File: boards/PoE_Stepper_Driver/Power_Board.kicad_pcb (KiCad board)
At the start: 2 copper layers, 86.4 x 40.6 mm, 13 parts, among them J5 48V In, J6 12V, 3V3 Out, U4 NCP1117, U5 E48SC12010

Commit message: finished power board fr
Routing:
- net +12V: track 11.1 -> 26.5 mm
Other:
- outline, holes or cut-outs redrawn
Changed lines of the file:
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@@
   (general
     (thickness 1.6)
-    (drawings 6)
-    (tracks 20)
+    (drawings 10)
+    (tracks 23)
     (zones 0)
     (modules 13)
@@
   )
   (setup
-    (last_trace_width 0.508)
+    (last_trace_width 1.524)
     (user_trace_width 0.2032)
     (user_trace_width 0.254)
@@
     (user_trace_width 1.524)
     (trace_clearance 0.2)
-    (zone_clearance 0.254)
+    (zone_clearance 0.127)
     (zone_45_only no)
     (trace_min 0.2)
@@
     )
   )
+  (gr_arc (start 92.837 22.352) (end 94.107 22.352) (angle -90) (layer Edge.Cuts) (width 0.05))
+  (gr_arc (start 92.837 60.452) (end 92.837 61.722) (angle -90) (layer Edge.Cuts) (width 0.05))
+  (gr_arc (start 9.017 60.452) (end 7.747 60.452) (angle -90) (layer Edge.Cuts) (width 0.05))
+  (gr_arc (start 9.017 22.352) (end 9.017 21.082) (angle -90) (layer Edge.Cuts) (width 0.05))
   (dimension 40.64 (width 0.15) (layer Dwgs.User)
     (gr_text "1.6000 in" (at -3.713 41.402 90) (layer Dwgs.User)
@@
     (arrow2b (pts (xy 7.747 13.462) (xy 8.873504 12.875579)))
   )
-  (gr_line (start 7.747 61.722) (end 7.747 21.082) (layer Edge.Cuts) (width 0.05))
-  (gr_line (start 94.107 61.722) (end 7.747 61.722) (layer Edge.Cuts) (width 0.05))
-  (gr_line (start 94.107 21.082) (end 94.107 61.722) (layer Edge.Cuts) (width 0.05))
-  (gr_line (start 7.747 21.082) (end 94.107 21.082) (layer Edge.Cuts) (width 0.05))
+  (gr_line (start 7.747 60.452) (end 7.747 22.352) (layer Edge.Cuts) (width 0.05))
+  (gr_line (start 92.837 61.722) (end 9.017 61.722) (layer Edge.Cuts) (width 0.05))
+  (gr_line (start 94.107 22.352) (end 94.107 60.452) (layer Edge.Cuts) (width 0.05))
+  (gr_line (start 9.017 21.082) (end 92.837 21.082) (layer Edge.Cuts) (width 0.05))
   (segment (start 81.051 37.084) (end 87.351 37.084) (width 1.524) (layer F.Cu) (net 2))
   (segment (start 85.48 35.213) (end 87.351 37.084) (width 1.27) (layer F.Cu) (net 2))
@@
   (segment (start 74.817 39.384) (end 81.051 39.384) (width 1.524) (layer F.Cu) (net 5))
   (segment (start 74.041 38.608) (end 74.817 39.384) (width 1.524) (layer F.Cu) (net 5))
+  (segment (start 69.889 34.798) (end 74.041 34.798) (width 1.524) (layer F.Cu) (net 5))
+  (segment (start 63.627 28.536) (end 69.889 34.798) (width 1.524) (layer F.Cu) (net 5))
+  (segment (start 63.627 26.162) (end 63.627 28.536) (width 1.524) (layer F.Cu) (net 5))
   (via (at 81.026 29.464) (size 0.8) (drill 0.4) (layers F.Cu B.Cu) (net 7))
   (segment (start 81.035 29.455) (end 81.026 29.464) (width 0.254) (layer F.Cu) (net 7))
@@
   (segment (start 76.971 28.194) (end 78.985 28.194) (width 0.508) (layer F.Cu) (net 8))
   (zone (net 1) (net_name VOUT-) (layer B.Cu) (hatch edge 0.508)
+    (priority 1)
     (connect_pads yes (clearance 0.127))
     (min_thickness 0.254)
@@
     (polygon
       (pts
-        (xy 49.657 80.772) (xy -4.953 80.772) (xy -4.953 -10.668) (xy 49.657 -10.668)
+        (xy 49.657 62.992) (xy -4.953 62.992) (xy -4.953 18.542) (xy 49.657 18.542)
       )
     )
   )
   (zone (net 3) (net_name VOUT+) (layer F.Cu) (hatch edge 0.508)
+    (priority 1)
     (connect_pads yes (clearance 0.254))
     (min_thickness 0.254)
@@
     (polygon
       (pts
-        (xy 49.657 80.772) (xy -4.953 80.772) (xy -4.953 -10.668) (xy 49.657 -10.668)
+        (xy 49.657 62.992) (xy -4.953 62.992) (xy -4.953 18.542) (xy 49.657 18.542)
       )
     )
@@
     (polygon
       (pts
-        (xy 104.267 80.772) (xy 49.657 80.772) (xy 49.657 -10.668) (xy 104.267 -10.668)
+        (xy 104.267 62.992) (xy 49.657 62.992) (xy 49.657 18.542) (xy 104.267 18.542)
       )
     )
@@
     (polygon
       (pts
-        (xy 104.267 80.772) (xy 49.657 80.772) (xy 49.657 -10.668) (xy 104.267 -10.668)
+        (xy 104.267 62.992) (xy 49.657 62.992) (xy 49.657 18.542) (xy 104.267 18.542)
       )
     )

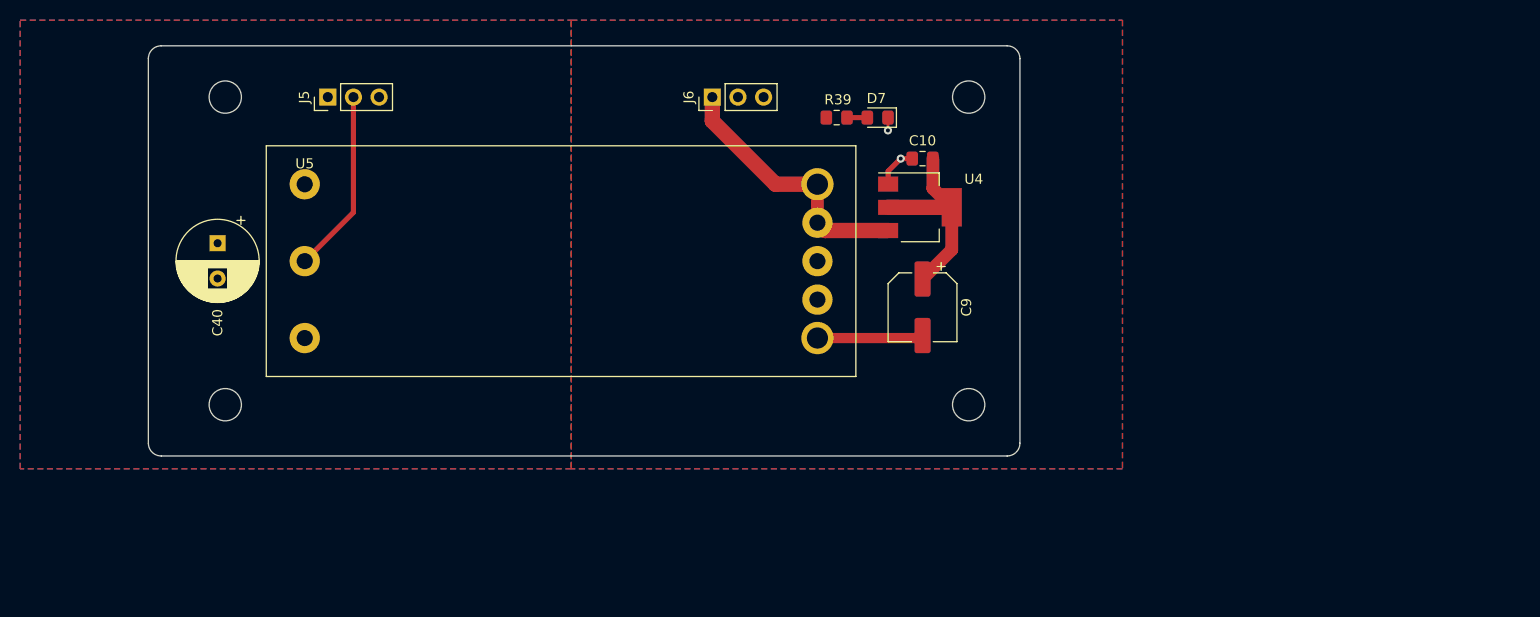
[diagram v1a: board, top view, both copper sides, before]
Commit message: done routing phy signals to mcu
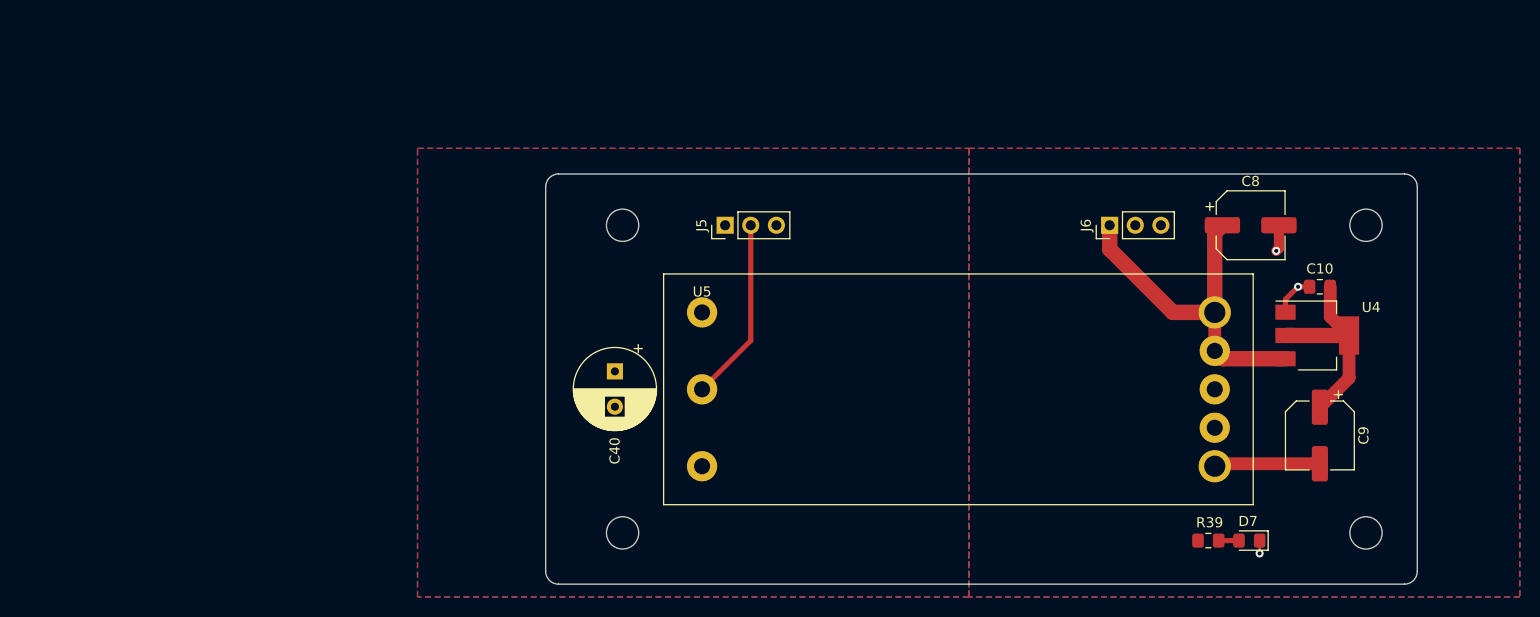
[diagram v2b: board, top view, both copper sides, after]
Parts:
- removed the REF** at (15.4, 26.2)
- removed the REF** at (15.4, 56.6)
- removed the REF** at (89.0, 56.6)
- added C8: 10uF, Capacitor_SMD:CP_Elec_6.3x5.4, F.Cu at (117.0, 38.9)
- added REF**: MountingHole_3.2mm_M3, MountingHole:MountingHole_3.2mm_M3, F.Cu at (54.7, 38.9)
- added REF**: MountingHole_3.2mm_M3, MountingHole:MountingHole_3.2mm_M3, F.Cu at (54.7, 69.3)
- added REF**: MountingHole_3.2mm_M3, MountingHole:MountingHole_3.2mm_M3, F.Cu at (128.4, 69.3)
- moved D7 55.8 mm to (116.8, 70.1)
- moved R39 55.8 mm to (112.8, 70.1)
- moved C10 41.4 mm to (123.8, 45.0)
- moved C40 41.4 mm to (54.0, 53.3)
- moved C9 41.4 mm to (123.8, 59.7)
- moved J5 41.4 mm to (64.9, 38.9)
- moved U4 41.4 mm to (123.6, 49.8)
- moved J6 41.4 mm to (103.0, 38.9)
- moved U5 41.4 mm to (62.6, 47.5)
- moved REF** 41.4 mm to (128.4, 38.9)
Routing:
- net +12V: track 26.5 -> 35.5 mm
- net GND: track 16.0 -> 18.6 mm, vias 2 -> 3

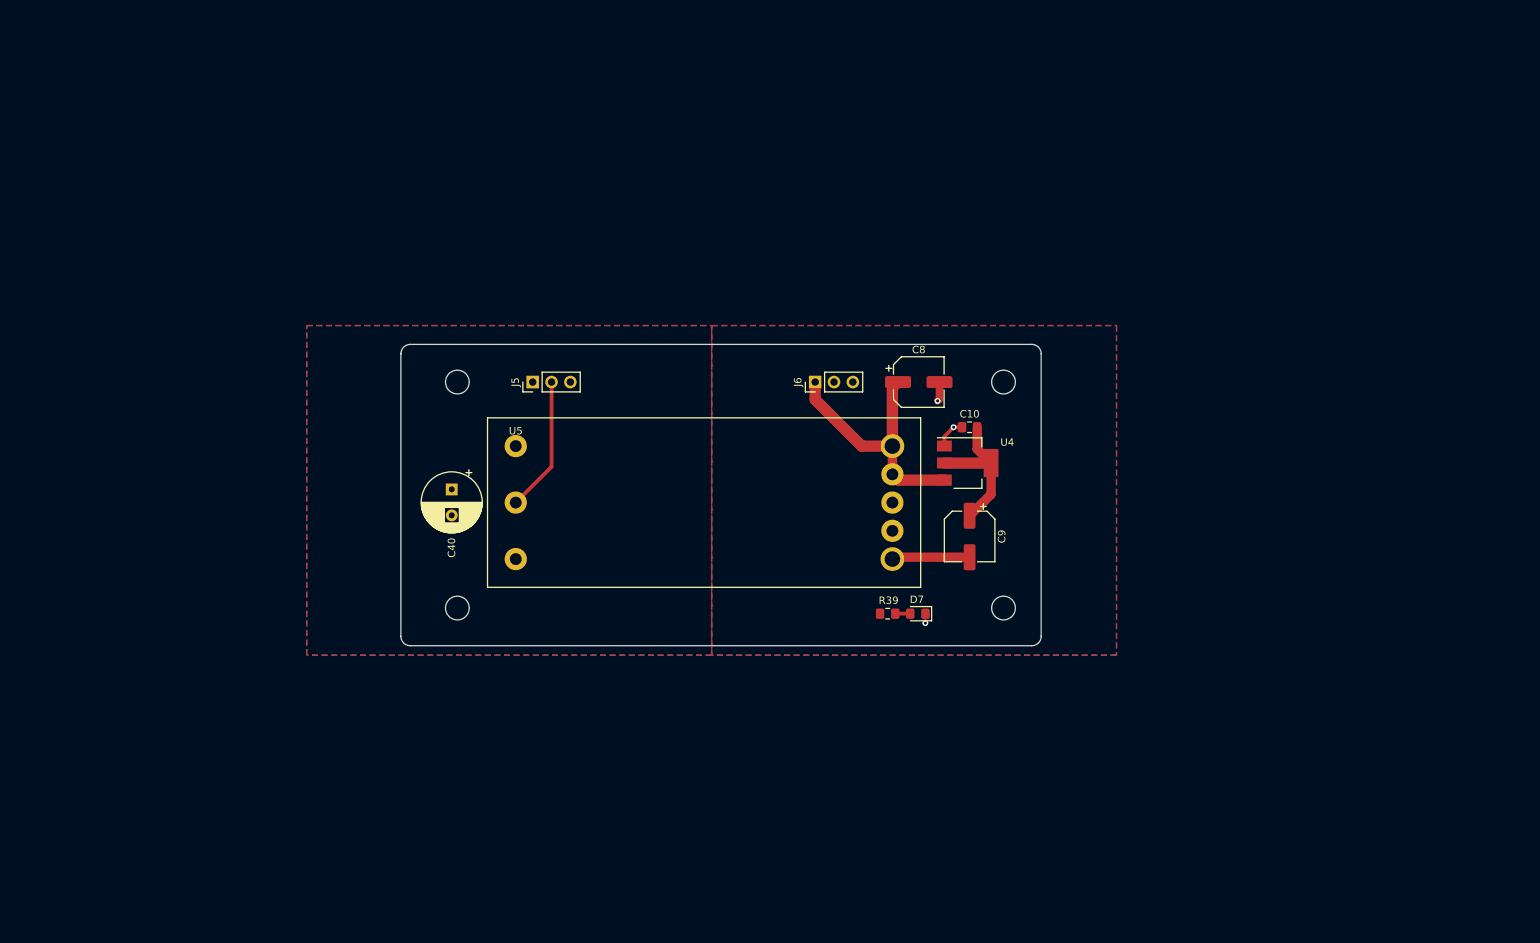
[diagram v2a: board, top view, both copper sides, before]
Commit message: added silkscreen info
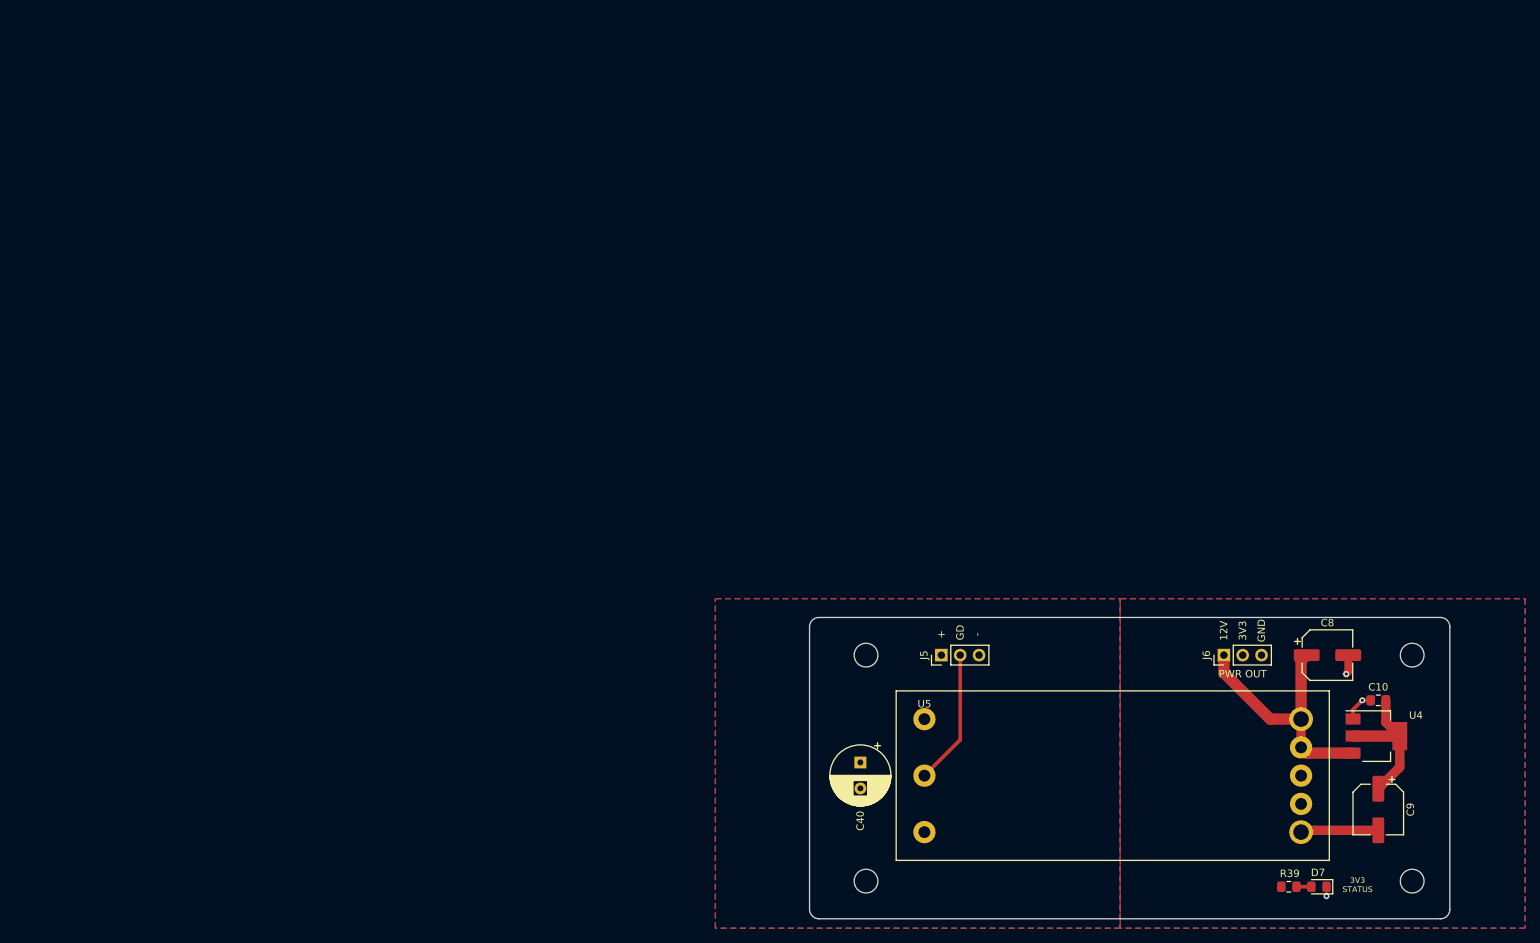
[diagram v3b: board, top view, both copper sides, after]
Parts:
- removed the REF** at (54.7, 38.9)
- removed the REF** at (54.7, 69.3)
- removed the REF** at (128.4, 69.3)
- added REF**: MountingHole_3.2mm_M3, MountingHole:MountingHole_3.2mm_M3, F.Cu at (109.9, 75.7)
- added REF**: MountingHole_3.2mm_M3, MountingHole:MountingHole_3.2mm_M3, F.Cu at (109.9, 106.2)
- added REF**: MountingHole_3.2mm_M3, MountingHole:MountingHole_3.2mm_M3, F.Cu at (183.5, 106.2)
- J5: value 48V In -> PWR IN
- J6: value 12V, 3V3 Out -> PWR OUT
- moved U5 66.3 mm to (117.7, 84.3)
- moved C10 66.3 mm to (178.9, 81.8)
- moved C40 66.3 mm to (109.1, 90.2)
- moved C8 66.3 mm to (172.1, 75.7)
- moved C9 66.3 mm to (178.9, 96.5)
- moved J6 66.3 mm to (158.1, 75.7)
- moved U4 66.3 mm to (178.7, 86.6)
- moved J5 66.3 mm to (120.0, 75.7)
- moved REF** 66.3 mm to (183.5, 75.7)
- moved D7 65.4 mm to (170.9, 106.9)
- moved R39 65.4 mm to (166.9, 106.9)
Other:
- board text added: "3V3 STATUS"

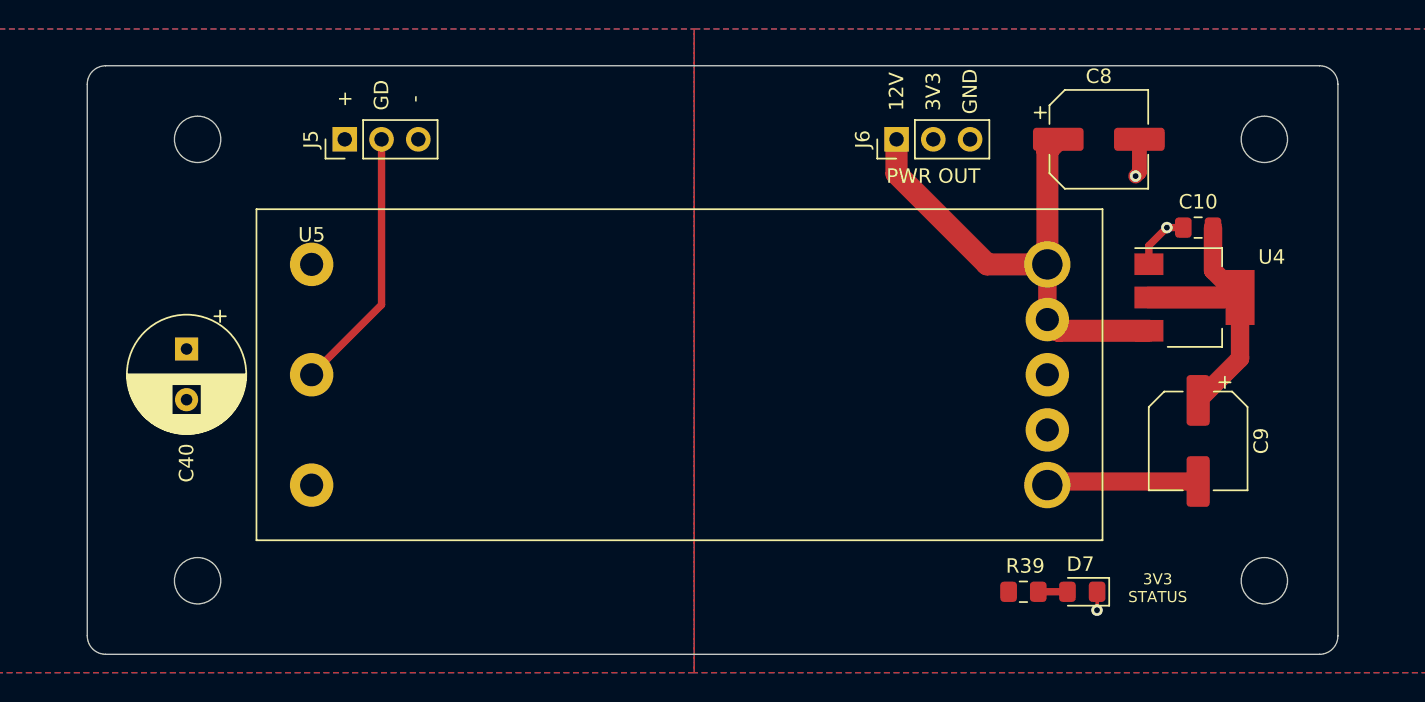
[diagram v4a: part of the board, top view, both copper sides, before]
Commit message: made rev2 board changes
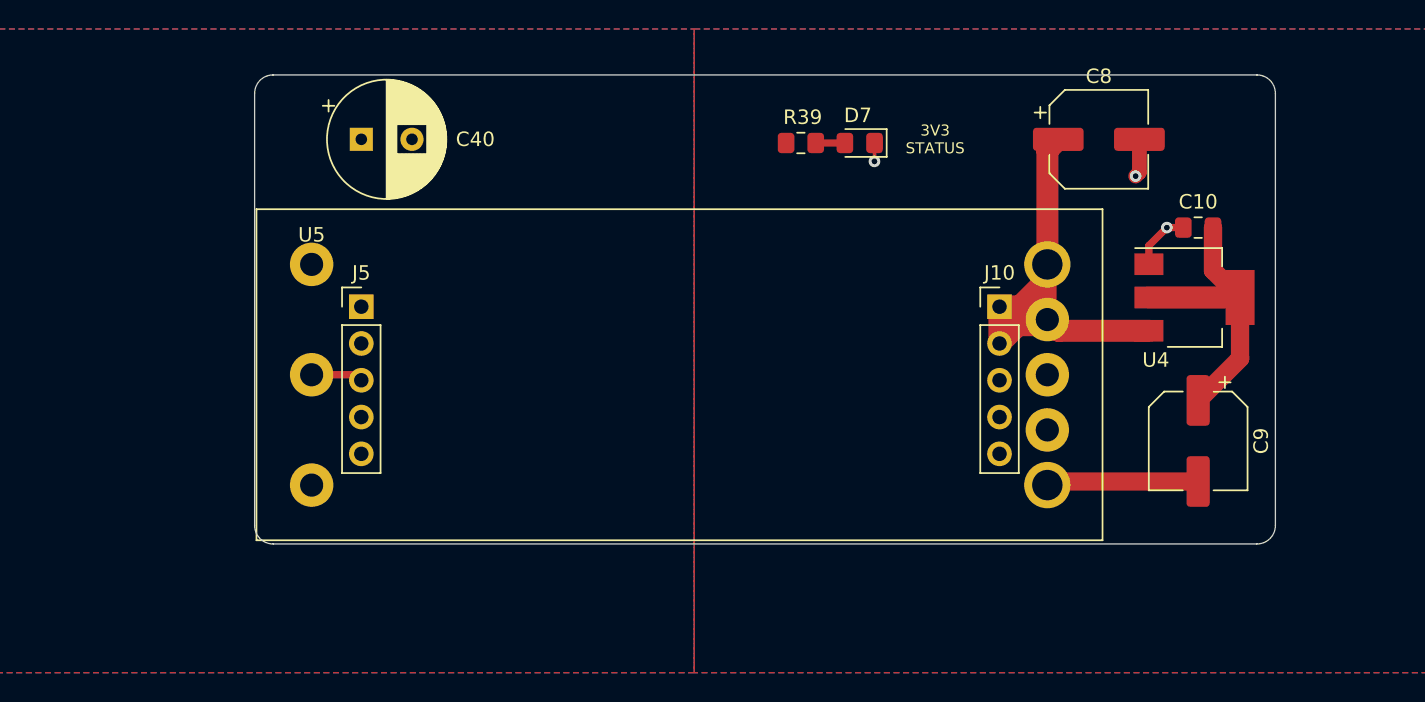
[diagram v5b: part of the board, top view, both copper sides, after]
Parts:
- removed J6: PWR OUT, Connector_PinHeader_2.54mm:PinHeader_1x03_P2.54mm_Vertical
- removed REF** (x4): MountingHole_3.2mm_M3, MountingHole:MountingHole_3.2mm_M3
- added J10: Converter Output, Connector_PinHeader_2.54mm:PinHeader_1x05_P2.54mm_Vertical, F.Cu at (165.2, 87.2)
- J5: value PWR IN -> Converter Input; footprint Connector_PinHeader_2.54mm:PinHeader_1x03_P2.54mm_Vertical -> Connector_PinHeader_2.54mm:PinHeader_1x05_P2.54mm_Vertical
- moved D7 34.6 mm to (155.6, 75.9)
- moved R39 34.6 mm to (151.5, 75.9)
- moved C40 18.8 mm to (121.2, 75.7), turned to 0 degrees
- moved J5 11.6 mm to (121.2, 87.2), turned to 0 degrees
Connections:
- J5 pad 2: PWRGD -> VOUT+
- J5 pad 3: VOUT- -> PWRGD
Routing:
- net PWRGD: track 18.3 -> 3.59 mm
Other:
- board size 86.4 x 40.6 mm -> 70.5 x 32.4 mm
